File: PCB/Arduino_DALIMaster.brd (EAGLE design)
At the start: 100 x 80 mm, 13 parts, among them J1 22-27-2021-02, U1 ARDUINOR3-BPLACE

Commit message: DRC
DRC and fixing
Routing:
- net VCC: track 142.5 -> 129.6 mm, vias 0 -> 1
- net GND: track 144.8 -> 136.8 mm, vias 0 -> 2
- net CHLVL3: track 39.9 -> 40.6 mm

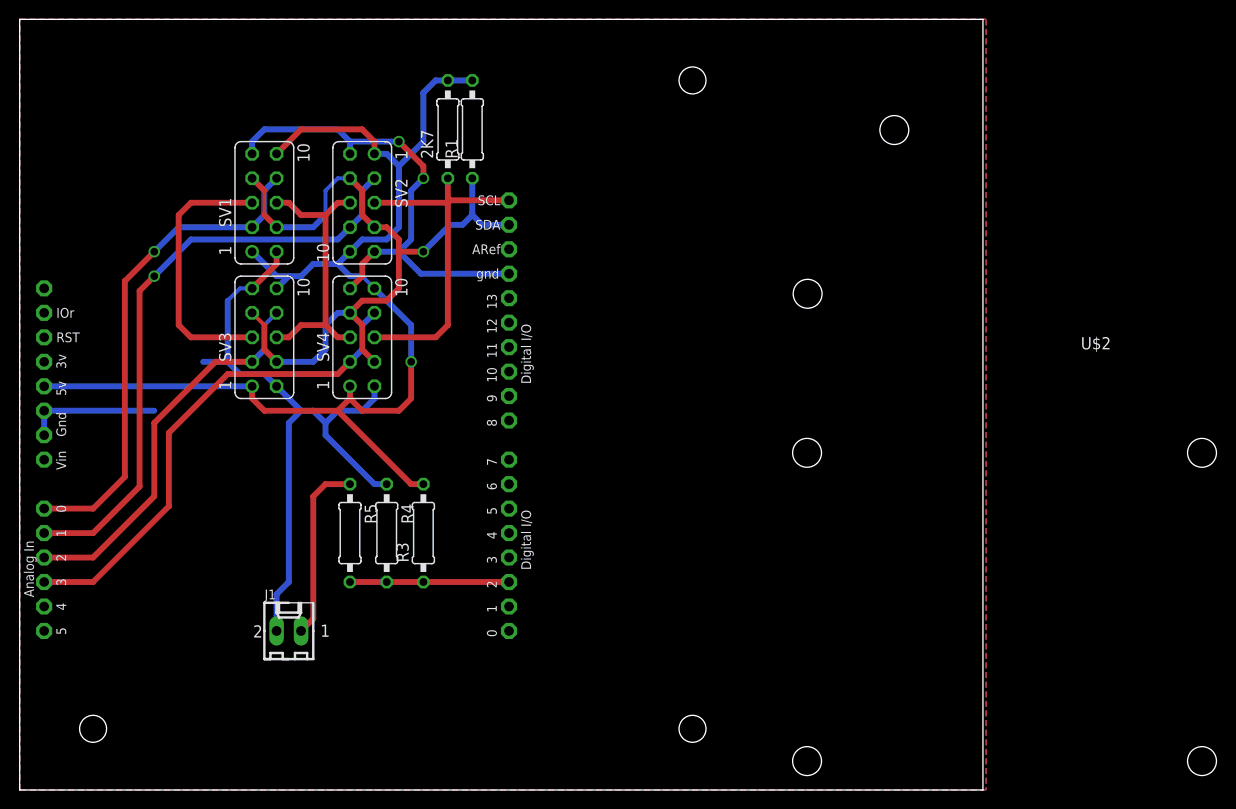
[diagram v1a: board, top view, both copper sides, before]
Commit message: SMT parts and rerouting
replaced all wired passives with 0603 SMT packages, rewired some of the
connections, reduced board size to 80x90mm
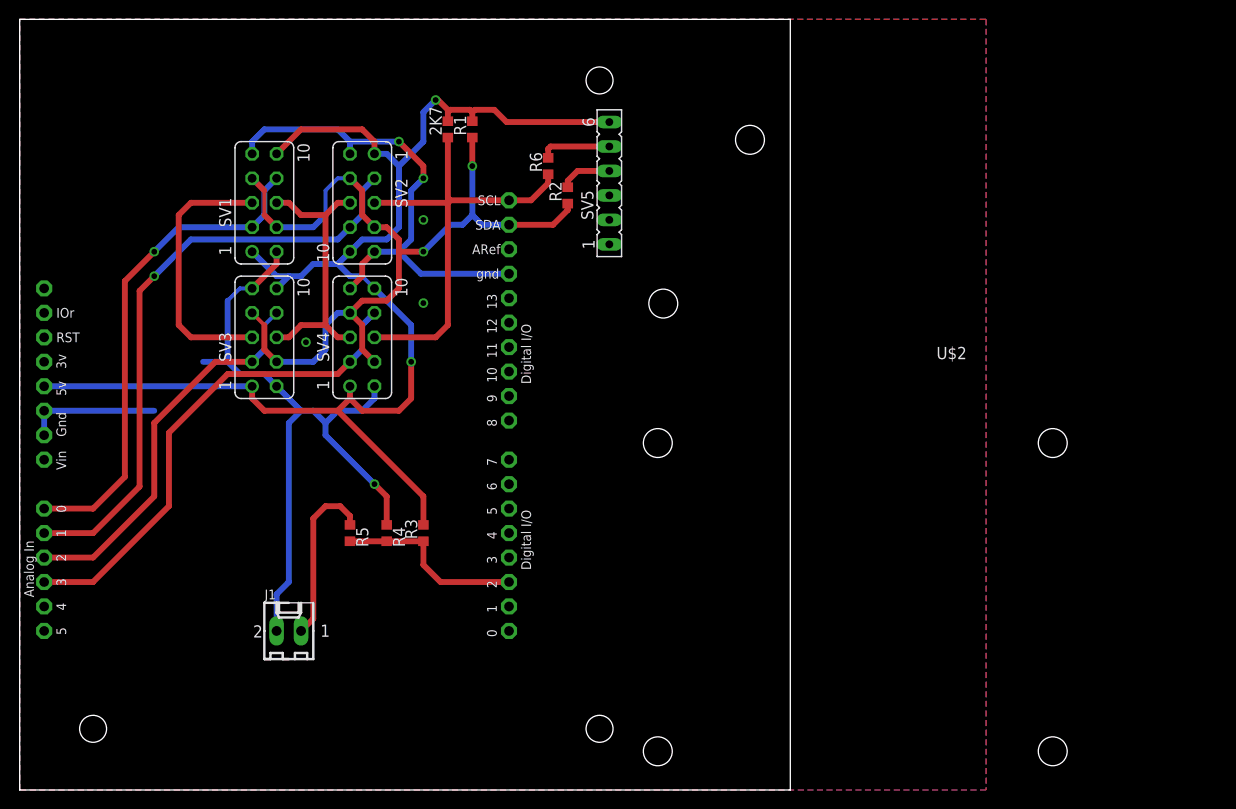
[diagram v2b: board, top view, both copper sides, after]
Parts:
- added R2, R6: 330/0603/5%, rcl:R0603
- added SV5: (no value), con-lsta:FE06
- 2K7, R1, R3, R4, R5: device rcl:0207/10 -> rcl:R0603
- moved U$1 15.5 mm to (63.2, 1.02)
- moved U$2 15.0 mm to (99.3, 79.0)
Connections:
- new net N$2: SV5.1
- new net N$3: SV5.2
- new net N$5: R2.2, SV5.4
- new net N$6: R6.2, SV5.5
- net GND: now also SV5.3
- net SCL: now also R6.1
- net SDA: now also R2.1
- net VCC: now also SV5.6
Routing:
- net VCC: track 129.6 -> 148.6 mm, vias 1 -> 2
- net SDA: track 78.5 -> 90.1 mm, vias 1 -> 2
- net SCL: track 93.8 -> 103.8 mm
- net N$6: track 0.00 -> 7.38 mm
- net N$5: track 0.00 -> 5.41 mm
- net GND: track 136.8 -> 140.2 mm, vias 2 -> 6
- net INTERRUPTPIN_DIM: track 16.5 -> 19.7 mm
- net N$1: track 18.8 -> 17.9 mm
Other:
- board size 100 x 80 mm -> 80 x 80 mm
